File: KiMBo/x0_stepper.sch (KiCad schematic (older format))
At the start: 25 parts, among them U14 TMC2130

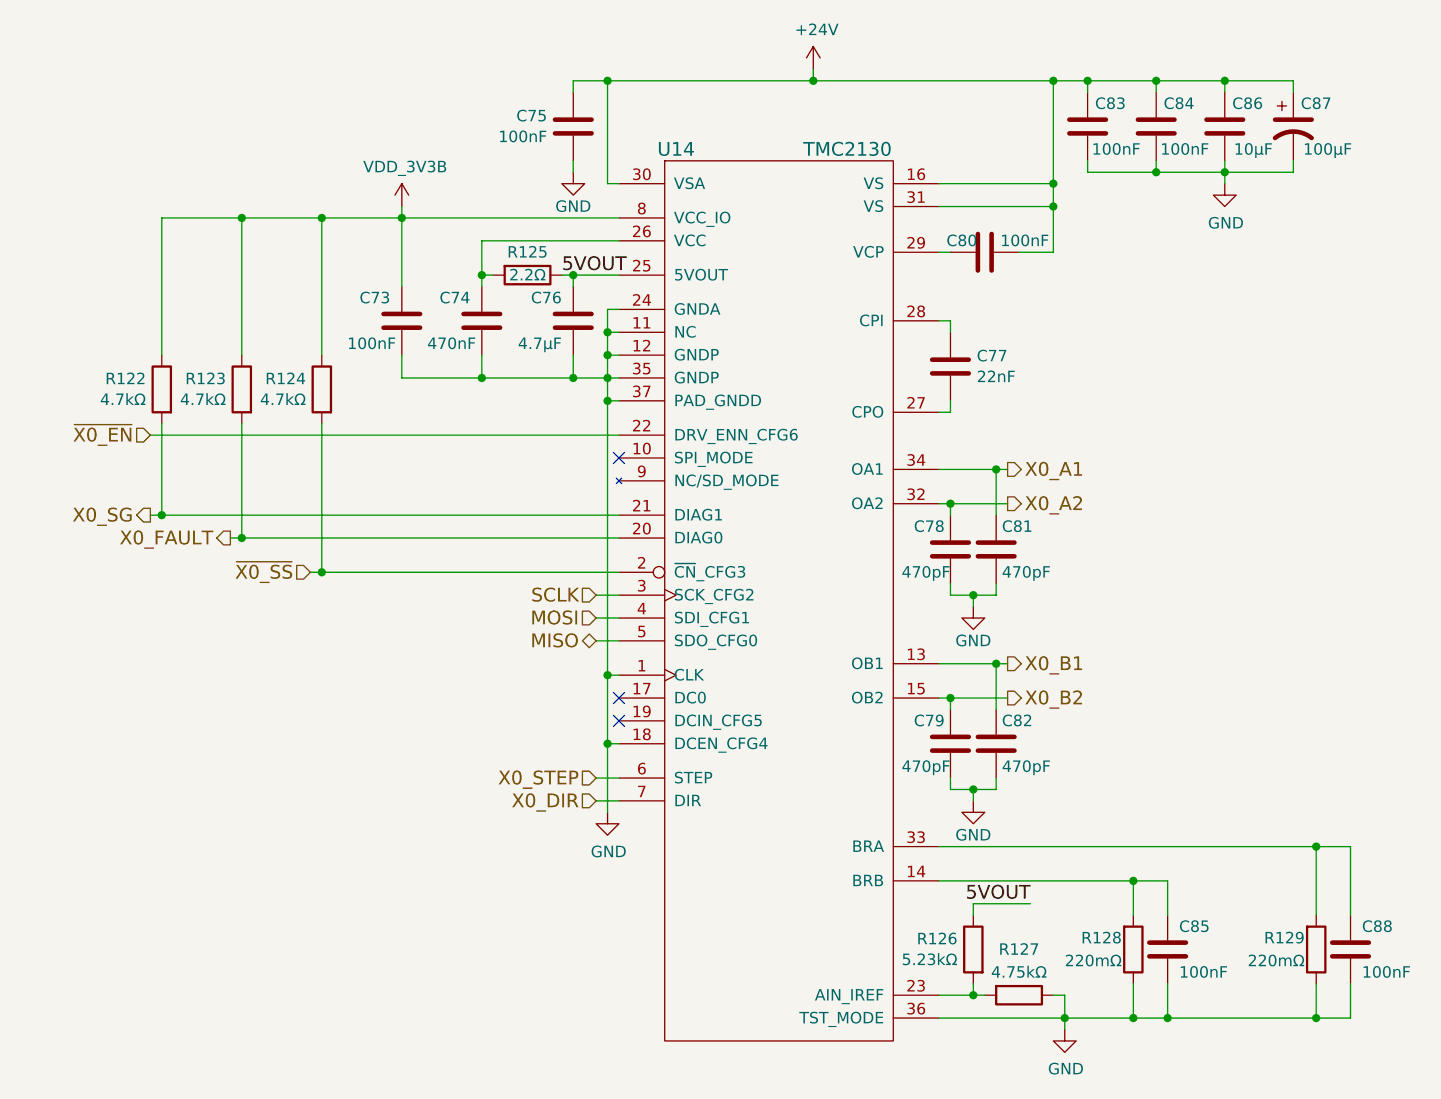
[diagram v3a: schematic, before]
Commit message: Add ferrite beads to the 5V and 3V pins at the SPI connectors
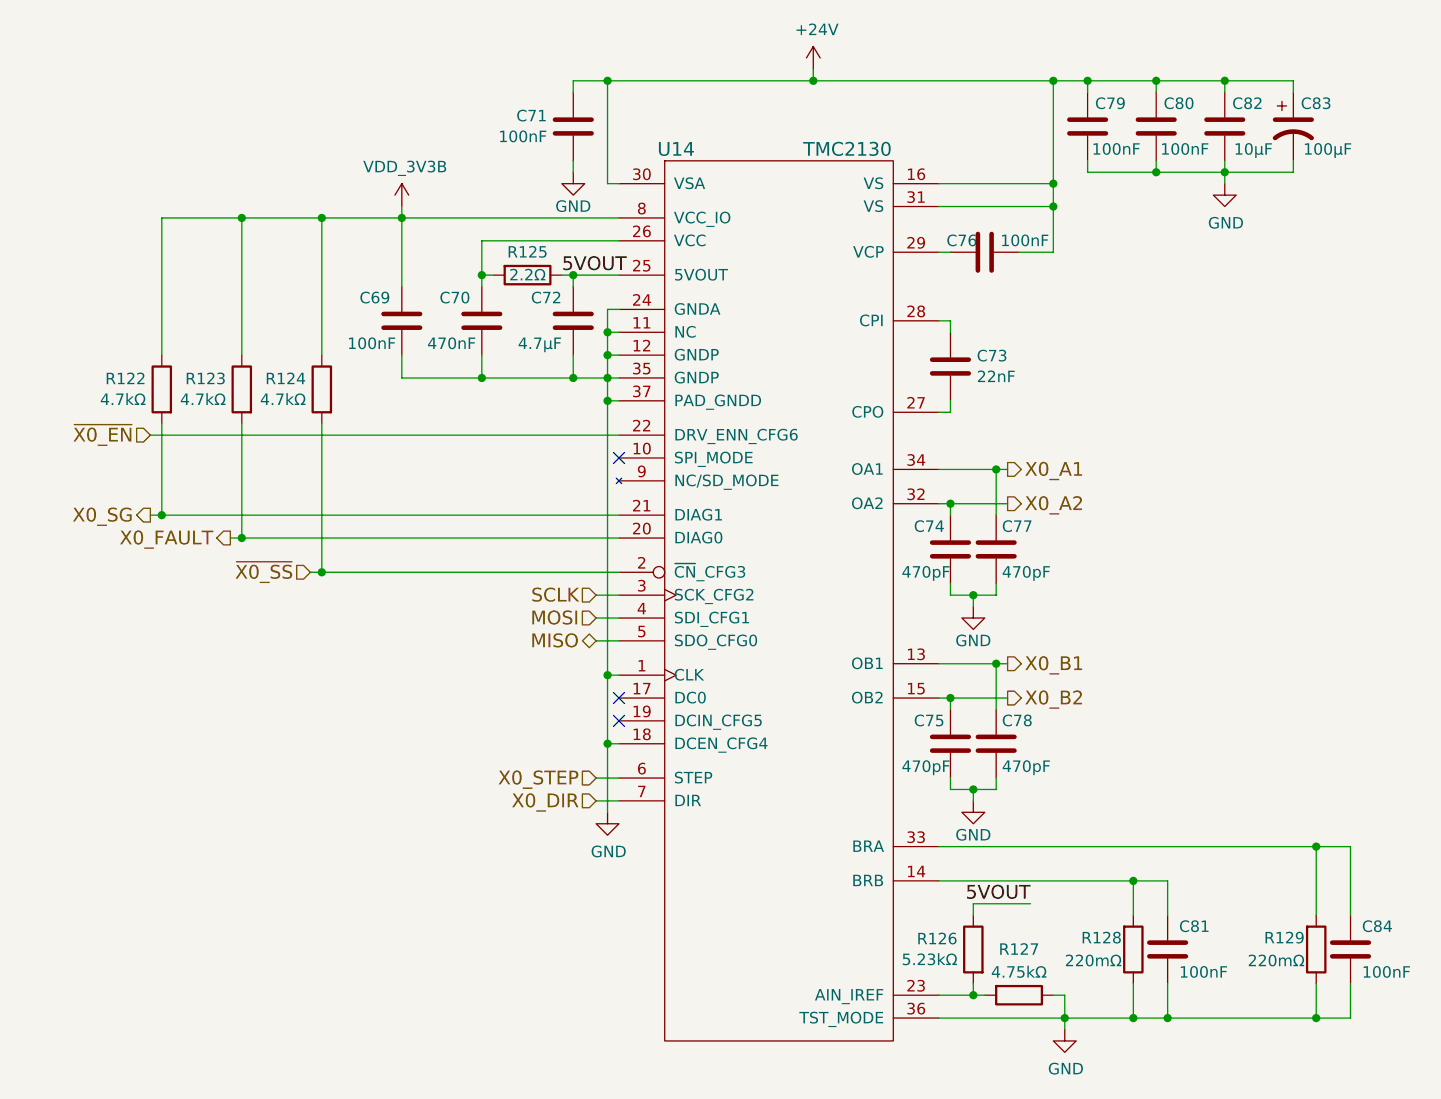
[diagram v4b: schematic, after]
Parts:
- renumbered C73 to C69, C74 to C70, C75 to C71, C76 to C72, C77 to C73, C78 to C74, C79 to C75, C80 to C76, C81 to C77, C82 to C78, C83 to C79, C84 to C80, C85 to C81, C86 to C82, C87 to C83, C88 to C84
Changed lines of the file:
@@
 X0_SG
 $Comp
-L C C75
+L C C71
 U 1 1 5BA7E13B
 P 7500 3100
-F 0 "C75" H 7386 3054 50  0000 R CNN
+F 0 "C71" H 7386 3054 50  0000 R CNN
 F 1 "100nF" H 7386 3145 50  0000 R CNN
 F 2 "Capacitors_SMD:C_0603" H 7538 2950 50  0001 C CNN
@@
 $EndComp
 $Comp
-L C C80
+L C C76
 U 1 1 5BA7E13C
 P 9300 3650
-F 0 "C80" V 9250 3550 50  0000 C CNN
+F 0 "C76" V 9250 3550 50  0000 C CNN
 F 1 "100nF" V 9250 3825 50  0000 C CNN
 F 2 "Capacitors_SMD:C_0603" H 9338 3500 50  0001 C CNN
@@
 $EndComp
 $Comp
-L CP1 C87
+L CP1 C83
 U 1 1 58C092C4
 P 10650 3100
-F 0 "C87" H 10750 3200 50  0000 C CNN
+F 0 "C83" H 10750 3200 50  0000 C CNN
 F 1 "100μF" H 10800 3000 50  0000 C CNN
 F 2 "Capacitors_SMD:c_elec_8x10" H 10650 3100 50  0001 C CNN
@@
 $EndComp
 $Comp
-L C C83
+L C C79
 U 1 1 58C092CB
 P 9750 3100
-F 0 "C83" H 9650 3200 50  0000 C CNN
+F 0 "C79" H 9650 3200 50  0000 C CNN
 F 1 "100nF" H 9625 3000 50  0000 C CNN
 F 2 "Capacitors_SMD:C_0603" H 9788 2950 50  0001 C CNN
@@
 $EndComp
 $Comp
-L GND #PWR0173
+L GND #PWR0170
 U 1 1 58C092D2
 P 7500 3300
-F 0 "#PWR0173" H 7500 3050 50  0001 C CNN
+F 0 "#PWR0170" H 7500 3050 50  0001 C CNN
 F 1 "GND" H 7500 3150 50  0000 C CNN
 F 2 "" H 7500 3300 50  0000 C CNN
@@
 $EndComp
 $Comp
-L C C84
+L C C80
 U 1 1 5BA7E140
 P 10050 3100
-F 0 "C84" H 9950 3200 50  0000 C CNN
+F 0 "C80" H 9950 3200 50  0000 C CNN
 F 1 "100nF" H 9925 3000 50  0000 C CNN
 F 2 "Capacitors_SMD:C_0603" H 10088 2950 50  0001 C CNN
@@
 $EndComp
 $Comp
-L GND #PWR0174
+L GND #PWR0171
 U 1 1 5BA7E141
 P 10350 3350
-F 0 "#PWR0174" H 10350 3100 50  0001 C CNN
+F 0 "#PWR0171" H 10350 3100 50  0001 C CNN
 F 1 "GND" H 10355 3177 50  0000 C CNN
 F 2 "" H 10350 3350 50  0000 C CNN
@@
 $EndComp
 $Comp
-L +24V #PWR0175
+L +24V #PWR0172
 U 1 1 58C092E5
 P 8550 2850
-F 0 "#PWR0175" H 8550 2700 50  0001 C CNN
+F 0 "#PWR0172" H 8550 2700 50  0001 C CNN
 F 1 "+24V" H 8565 3023 50  0000 C CNN
 F 2 "" H 8550 2850 50  0000 C CNN
@@
 $EndComp
 $Comp
-L C C77
+L C C73
 U 1 1 58C092EB
 P 9150 4150
-F 0 "C77" H 9265 4196 50  0000 L CNN
+F 0 "C73" H 9265 4196 50  0000 L CNN
 F 1 "22nF" H 9265 4105 50  0000 L CNN
 F 2 "Capacitors_SMD:C_0603" H 9188 4000 50  0001 C CNN
@@
 $EndComp
 $Comp
-L GND #PWR0176
+L GND #PWR0173
 U 1 1 5BA7E146
 P 9650 7050
-F 0 "#PWR0176" H 9650 6800 50  0001 C CNN
+F 0 "#PWR0173" H 9650 6800 50  0001 C CNN
 F 1 "GND" H 9655 6877 50  0000 C CNN
 F 2 "" H 9650 7050 50  0000 C CNN
@@
 $EndComp
 $Comp
-L C C74
+L C C70
 U 1 1 5BA7E148
 P 7100 3950
-F 0 "C74" H 7150 4050 50  0000 L CNN
+F 0 "C70" H 7150 4050 50  0000 L CNN
 F 1 "470nF" H 7125 3850 50  0000 L CNN
 F 2 "Capacitors_SMD:C_0603" H 7138 3800 50  0001 C CNN
@@
 NoConn ~ 7700 5700
 $Comp
-L GND #PWR0177
+L GND #PWR0174
 U 1 1 5BA7E149
 P 7650 6100
-F 0 "#PWR0177" H 7650 5850 50  0001 C CNN
+F 0 "#PWR0174" H 7650 5850 50  0001 C CNN
 F 1 "GND" H 7655 5927 50  0000 C CNN
 F 2 "" H 7650 6100 50  0000 C CNN
@@
 $EndComp
 $Comp
-L C C85
+L C C81
 U 1 1 5BA7E14A
 P 10100 6700
-F 0 "C85" H 10150 6800 50  0000 L CNN
+F 0 "C81" H 10150 6800 50  0000 L CNN
 F 1 "100nF" H 10150 6600 50  0000 L CNN
 F 2 "Capacitors_SMD:C_0603" H 10138 6550 50  0001 C CNN
@@
 NoConn ~ 7700 4550
 $Comp
-L C C76
+L C C72
 U 1 1 5BA7E14C
 P 7500 3950
-F 0 "C76" H 7550 4050 50  0000 L CNN
+F 0 "C72" H 7550 4050 50  0000 L CNN
 F 1 "4.7μF" H 7550 3850 50  0000 L CNN
 F 2 "Capacitors_SMD:C_0603" H 7538 3800 50  0001 C CNN
@@
 $EndComp
 $Comp
-L C C88
+L C C84
 U 1 1 58C0935A
 P 10900 6700
-F 0 "C88" H 10950 6800 50  0000 L CNN
+F 0 "C84" H 10950 6800 50  0000 L CNN
 F 1 "100nF" H 10950 6600 50  0000 L CNN
 F 2 "Capacitors_SMD:C_0603" H 10938 6550 50  0001 C CNN
@@
 $EndComp
 $Comp
-L C C78
+L C C74
 U 1 1 58C09363
 P 9150 4950
-F 0 "C78" H 9175 5050 50  0000 L CNN
+F 0 "C74" H 9175 5050 50  0000 L CNN
 F 1 "470pF" H 9150 4850 50  0000 L CNN
 F 2 "Capacitors_SMD:C_0603" H 9188 4800 50  0001 C CNN
@@
 $EndComp
 $Comp
-L GND #PWR0178
+L GND #PWR0175
 U 1 1 58C0936A
 P 9250 5200
-F 0 "#PWR0178" H 9250 4950 50  0001 C CNN
+F 0 "#PWR0175" H 9250 4950 50  0001 C CNN
 F 1 "GND" H 9250 5050 50  0000 C CNN
 F 2 "" H 9250 5200 50  0000 C CNN
@@
 $EndComp
 $Comp
-L C C81
+L C C77
 U 1 1 58C09370
 P 9350 4950
-F 0 "C81" H 9375 5050 50  0000 L CNN
+F 0 "C77" H 9375 5050 50  0000 L CNN
 F 1 "470pF" H 9375 4850 50  0000 L CNN
 F 2 "Capacitors_SMD:C_0603" H 9388 4800 50  0001 C CNN
@@
 $EndComp
 $Comp
-L C C79
+L C C75
 U 1 1 5BA7E154
 P 9150 5800
-F 0 "C79" H 9175 5900 50  0000 L CNN
+F 0 "C75" H 9175 5900 50  0000 L CNN
 F 1 "470pF" H 9150 5700 50  0000 L CNN
 F 2 "Capacitors_SMD:C_0603" H 9188 5650 50  0001 C CNN
@@
 $EndComp
 $Comp
-L GND #PWR0179
+L GND #PWR0176
 U 1 1 58C0937E
 P 9250 6050
-F 0 "#PWR0179" H 9250 5800 50  0001 C CNN
+F 0 "#PWR0176" H 9250 5800 50  0001 C CNN
 F 1 "GND" H 9250 5900 50  0000 C CNN
 F 2 "" H 9250 6050 50  0000 C CNN
@@
 $EndComp
 $Comp
-L C C82
+L C C78
 U 1 1 58C09384
 P 9350 5800
-F 0 "C82" H 9375 5900 50  0000 L CNN
+F 0 "C78" H 9375 5900 50  0000 L CNN
 F 1 "470pF" H 9375 5700 50  0000 L CNN
 F 2 "Capacitors_SMD:C_0603" H 9388 5650 50  0001 C CNN
@@
 Connection ~ 6050 3500
 $Comp
-L C C86
+L C C82
 U 1 1 5BA7E159
 P 10350 3100
-F 0 "C86" H 10250 3200 50  0000 C CNN
+F 0 "C82" H 10250 3200 50  0000 C CNN
 F 1 "10μF" H 10225 3000 50  0000 C CNN
 F 2 "Capacitors_SMD:C_0805" H 10388 2950 50  0001 C CNN
@@
 	5700 3500 7700 3500
 $Comp
-L VDD_3V3B #PWR0180
+L VDD_3V3B #PWR0177
 U 1 1 5A2FF856
 P 6750 3450
-F 0 "#PWR0180" H 6750 3300 50  0001 C CNN
+F 0 "#PWR0177" H 6750 3300 50  0001 C CNN
 F 1 "VDD_3V3B" H 6765 3623 50  0000 C CNN
 F 2 "" H 6750 3450 50  0000 C CNN
@@
 $EndComp
 $Comp
-L C C73
+L C C69
 U 1 1 5A89853C
 P 6750 3950
-F 0 "C73" H 6800 4050 50  0000 L CNN
+F 0 "C69" H 6800 4050 50  0000 L CNN
 F 1 "100nF" H 6775 3850 50  0000 L CNN
 F 2 "Capacitors_SMD:C_0603" H 6788 3800 50  0001 C CNN

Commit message: Complete SPI, ADC, and Endstop header layout/position, add zone around the SiP
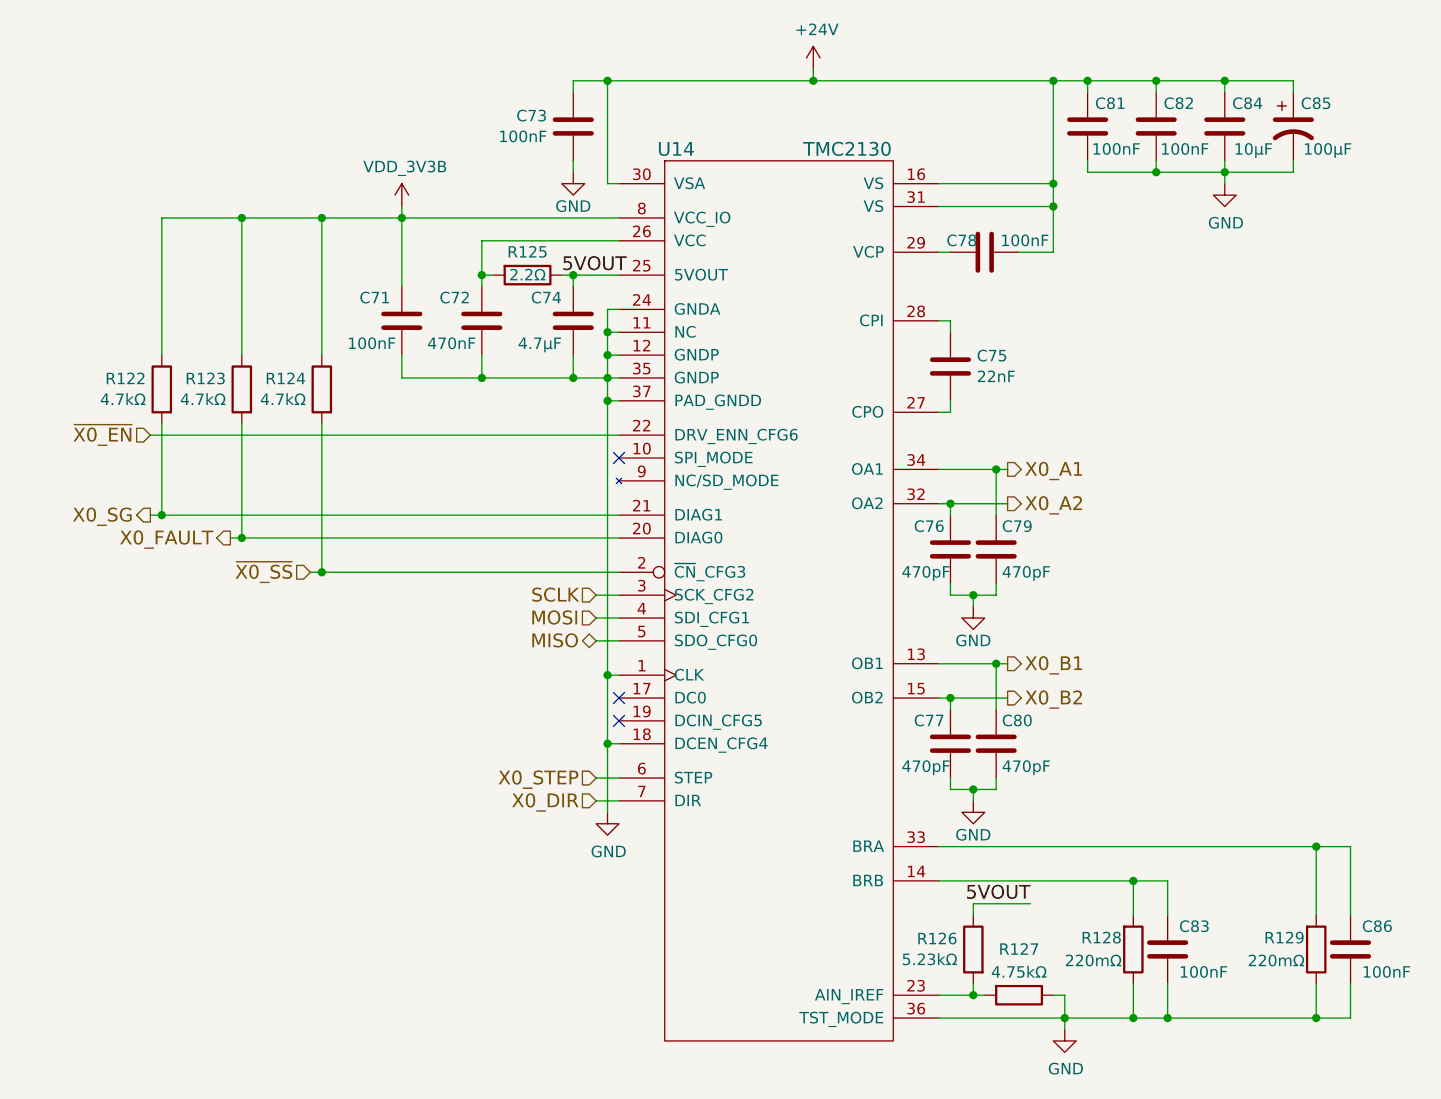
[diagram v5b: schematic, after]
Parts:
- renumbered C69 to C71, C70 to C72, C71 to C73, C72 to C74, C73 to C75, C74 to C76, C75 to C77, C76 to C78, C77 to C79, C78 to C80, C79 to C81, C80 to C82, C81 to C83, C82 to C84, C83 to C85, C84 to C86
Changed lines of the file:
@@
 X0_SG
 $Comp
-L C C71
+L C C73
 U 1 1 5BA7E13B
 P 7500 3100
-F 0 "C71" H 7386 3054 50  0000 R CNN
+F 0 "C73" H 7386 3054 50  0000 R CNN
 F 1 "100nF" H 7386 3145 50  0000 R CNN
 F 2 "Capacitors_SMD:C_0603" H 7538 2950 50  0001 C CNN
@@
 $EndComp
 $Comp
-L C C76
+L C C78
 U 1 1 5BA7E13C
 P 9300 3650
-F 0 "C76" V 9250 3550 50  0000 C CNN
+F 0 "C78" V 9250 3550 50  0000 C CNN
 F 1 "100nF" V 9250 3825 50  0000 C CNN
 F 2 "Capacitors_SMD:C_0603" H 9338 3500 50  0001 C CNN
@@
 $EndComp
 $Comp
-L CP1 C83
+L CP1 C85
 U 1 1 58C092C4
 P 10650 3100
-F 0 "C83" H 10750 3200 50  0000 C CNN
+F 0 "C85" H 10750 3200 50  0000 C CNN
 F 1 "100μF" H 10800 3000 50  0000 C CNN
 F 2 "Capacitors_SMD:c_elec_8x10" H 10650 3100 50  0001 C CNN
@@
 $EndComp
 $Comp
-L C C79
+L C C81
 U 1 1 58C092CB
 P 9750 3100
-F 0 "C79" H 9650 3200 50  0000 C CNN
+F 0 "C81" H 9650 3200 50  0000 C CNN
 F 1 "100nF" H 9625 3000 50  0000 C CNN
 F 2 "Capacitors_SMD:C_0603" H 9788 2950 50  0001 C CNN
@@
 $EndComp
 $Comp
-L GND #PWR0170
+L GND #PWR0172
 U 1 1 58C092D2
 P 7500 3300
-F 0 "#PWR0170" H 7500 3050 50  0001 C CNN
+F 0 "#PWR0172" H 7500 3050 50  0001 C CNN
 F 1 "GND" H 7500 3150 50  0000 C CNN
 F 2 "" H 7500 3300 50  0000 C CNN
@@
 $EndComp
 $Comp
-L C C80
+L C C82
 U 1 1 5BA7E140
 P 10050 3100
-F 0 "C80" H 9950 3200 50  0000 C CNN
+F 0 "C82" H 9950 3200 50  0000 C CNN
 F 1 "100nF" H 9925 3000 50  0000 C CNN
 F 2 "Capacitors_SMD:C_0603" H 10088 2950 50  0001 C CNN
@@
 $EndComp
 $Comp
-L GND #PWR0171
+L GND #PWR0173
 U 1 1 5BA7E141
 P 10350 3350
-F 0 "#PWR0171" H 10350 3100 50  0001 C CNN
+F 0 "#PWR0173" H 10350 3100 50  0001 C CNN
 F 1 "GND" H 10355 3177 50  0000 C CNN
 F 2 "" H 10350 3350 50  0000 C CNN
@@
 $EndComp
 $Comp
-L +24V #PWR0172
+L +24V #PWR0174
 U 1 1 58C092E5
 P 8550 2850
-F 0 "#PWR0172" H 8550 2700 50  0001 C CNN
+F 0 "#PWR0174" H 8550 2700 50  0001 C CNN
 F 1 "+24V" H 8565 3023 50  0000 C CNN
 F 2 "" H 8550 2850 50  0000 C CNN
@@
 $EndComp
 $Comp
-L C C73
+L C C75
 U 1 1 58C092EB
 P 9150 4150
-F 0 "C73" H 9265 4196 50  0000 L CNN
+F 0 "C75" H 9265 4196 50  0000 L CNN
 F 1 "22nF" H 9265 4105 50  0000 L CNN
 F 2 "Capacitors_SMD:C_0603" H 9188 4000 50  0001 C CNN
@@
 $EndComp
 $Comp
-L GND #PWR0173
+L GND #PWR0175
 U 1 1 5BA7E146
 P 9650 7050
-F 0 "#PWR0173" H 9650 6800 50  0001 C CNN
+F 0 "#PWR0175" H 9650 6800 50  0001 C CNN
 F 1 "GND" H 9655 6877 50  0000 C CNN
 F 2 "" H 9650 7050 50  0000 C CNN
@@
 $EndComp
 $Comp
-L C C70
+L C C72
 U 1 1 5BA7E148
 P 7100 3950
-F 0 "C70" H 7150 4050 50  0000 L CNN
+F 0 "C72" H 7150 4050 50  0000 L CNN
 F 1 "470nF" H 7125 3850 50  0000 L CNN
 F 2 "Capacitors_SMD:C_0603" H 7138 3800 50  0001 C CNN
@@
 NoConn ~ 7700 5700
 $Comp
-L GND #PWR0174
+L GND #PWR0176
 U 1 1 5BA7E149
 P 7650 6100
-F 0 "#PWR0174" H 7650 5850 50  0001 C CNN
+F 0 "#PWR0176" H 7650 5850 50  0001 C CNN
 F 1 "GND" H 7655 5927 50  0000 C CNN
 F 2 "" H 7650 6100 50  0000 C CNN
@@
 $EndComp
 $Comp
-L C C81
+L C C83
 U 1 1 5BA7E14A
 P 10100 6700
-F 0 "C81" H 10150 6800 50  0000 L CNN
+F 0 "C83" H 10150 6800 50  0000 L CNN
 F 1 "100nF" H 10150 6600 50  0000 L CNN
 F 2 "Capacitors_SMD:C_0603" H 10138 6550 50  0001 C CNN
@@
 NoConn ~ 7700 4550
 $Comp
-L C C72
+L C C74
 U 1 1 5BA7E14C
 P 7500 3950
-F 0 "C72" H 7550 4050 50  0000 L CNN
+F 0 "C74" H 7550 4050 50  0000 L CNN
 F 1 "4.7μF" H 7550 3850 50  0000 L CNN
 F 2 "Capacitors_SMD:C_0603" H 7538 3800 50  0001 C CNN
@@
 $EndComp
 $Comp
-L C C84
+L C C86
 U 1 1 58C0935A
 P 10900 6700
-F 0 "C84" H 10950 6800 50  0000 L CNN
+F 0 "C86" H 10950 6800 50  0000 L CNN
 F 1 "100nF" H 10950 6600 50  0000 L CNN
 F 2 "Capacitors_SMD:C_0603" H 10938 6550 50  0001 C CNN
@@
 $EndComp
 $Comp
-L C C74
+L C C76
 U 1 1 58C09363
 P 9150 4950
-F 0 "C74" H 9175 5050 50  0000 L CNN
+F 0 "C76" H 9175 5050 50  0000 L CNN
 F 1 "470pF" H 9150 4850 50  0000 L CNN
 F 2 "Capacitors_SMD:C_0603" H 9188 4800 50  0001 C CNN
@@
 $EndComp
 $Comp
-L GND #PWR0175
+L GND #PWR0177
 U 1 1 58C0936A
 P 9250 5200
-F 0 "#PWR0175" H 9250 4950 50  0001 C CNN
+F 0 "#PWR0177" H 9250 4950 50  0001 C CNN
 F 1 "GND" H 9250 5050 50  0000 C CNN
 F 2 "" H 9250 5200 50  0000 C CNN
@@
 $EndComp
 $Comp
-L C C77
+L C C79
 U 1 1 58C09370
 P 9350 4950
-F 0 "C77" H 9375 5050 50  0000 L CNN
+F 0 "C79" H 9375 5050 50  0000 L CNN
 F 1 "470pF" H 9375 4850 50  0000 L CNN
 F 2 "Capacitors_SMD:C_0603" H 9388 4800 50  0001 C CNN
@@
 $EndComp
 $Comp
-L C C75
+L C C77
 U 1 1 5BA7E154
 P 9150 5800
-F 0 "C75" H 9175 5900 50  0000 L CNN
+F 0 "C77" H 9175 5900 50  0000 L CNN
 F 1 "470pF" H 9150 5700 50  0000 L CNN
 F 2 "Capacitors_SMD:C_0603" H 9188 5650 50  0001 C CNN
@@
 $EndComp
 $Comp
-L GND #PWR0176
+L GND #PWR0178
 U 1 1 58C0937E
 P 9250 6050
-F 0 "#PWR0176" H 9250 5800 50  0001 C CNN
+F 0 "#PWR0178" H 9250 5800 50  0001 C CNN
 F 1 "GND" H 9250 5900 50  0000 C CNN
 F 2 "" H 9250 6050 50  0000 C CNN
@@
 $EndComp
 $Comp
-L C C78
+L C C80
 U 1 1 58C09384
 P 9350 5800
-F 0 "C78" H 9375 5900 50  0000 L CNN
+F 0 "C80" H 9375 5900 50  0000 L CNN
 F 1 "470pF" H 9375 5700 50  0000 L CNN
 F 2 "Capacitors_SMD:C_0603" H 9388 5650 50  0001 C CNN
@@
 Connection ~ 6050 3500
 $Comp
-L C C82
+L C C84
 U 1 1 5BA7E159
 P 10350 3100
-F 0 "C82" H 10250 3200 50  0000 C CNN
+F 0 "C84" H 10250 3200 50  0000 C CNN
 F 1 "10μF" H 10225 3000 50  0000 C CNN
 F 2 "Capacitors_SMD:C_0805" H 10388 2950 50  0001 C CNN
@@
 	5700 3500 7700 3500
 $Comp
-L VDD_3V3B #PWR0177
+L VDD_3V3B #PWR0179
 U 1 1 5A2FF856
 P 6750 3450
-F 0 "#PWR0177" H 6750 3300 50  0001 C CNN
+F 0 "#PWR0179" H 6750 3300 50  0001 C CNN
 F 1 "VDD_3V3B" H 6765 3623 50  0000 C CNN
 F 2 "" H 6750 3450 50  0000 C CNN
@@
 $EndComp
 $Comp
-L C C69
+L C C71
 U 1 1 5A89853C
 P 6750 3950
-F 0 "C69" H 6800 4050 50  0000 L CNN
+F 0 "C71" H 6800 4050 50  0000 L CNN
 F 1 "100nF" H 6775 3850 50  0000 L CNN
 F 2 "Capacitors_SMD:C_0603" H 6788 3800 50  0001 C CNN
